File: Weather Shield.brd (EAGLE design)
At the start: 53.3 x 59.7 mm, 46 parts, among them J1 GP-635T, Q1 BSS138, Q2 BSS138, U1 ARDUINO_R3_SHIELD, U2 3.3V MIC5219, U3 ALS-PT19, U4 MPL3115A2LGA8, U5 HTU21D

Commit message: Initial commit
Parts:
- removed C1: 1uF, SparkFun:0603-CAP
- removed C13, C14: 10uF, SparkFun-Passives:EIA3216
- removed C2: 0.1uF, SparkFun:0603-CAP
- removed J1: GP-635T, SparkFun-Sensors:GP-635T
- removed JP2: External Batt Bckup, SparkFun-Connectors:1X02
- removed R10: 10K, SparkFun-Passives:0603-RES
- removed R7: 1K, SparkFun:0603-RES
- removed R8: 3.9K, SparkFun:0603-RES
- removed R9: 4.7K, SparkFun:0603-RES
- removed S2: Serial Select, SparkFun-Electromechanical:AYZ0202
- removed U1: ARDUINO_R3_SHIELD, SparkFun-Boards:UNO_R3_SHIELD
- removed U2: 3.3V MIC5219, SparkFun:SOT23-5
- removed U3: ALS-PT19, SparkFun-Sensors:ALS-PT19
- D1: value Blue -> Red
- moved JP10-DNP 50.6 mm to (52.1, 5.08), turned to 90 degrees
- moved LOGO1 46.6 mm to (3.81, 2.54)
- moved JP9-DNP 44.9 mm to (52.1, 21.6), turned to 90 degrees
- moved R16 37.6 mm to (36.8, 2.54), turned to 270 degrees
- moved R15 33.2 mm to (36.8, 6.35), turned to 270 degrees
- moved D9 32.7 mm to (39.4, 5.08), turned to 90 degrees
- moved R14 29.2 mm to (36.8, 10.2), turned to 90 degrees
- moved D10 28.2 mm to (39.4, 8.89), turned to 90 degrees
- moved R11 27.3 mm to (38.1, 26.7), turned to 270 degrees
- moved R12 25.9 mm to (35.6, 34.3), turned to 270 degrees
- moved R13 25.7 mm to (36.8, 14.0), turned to 270 degrees
- moved D7 24.1 mm to (39.4, 12.7), turned to 90 degrees
- moved R4 23.3 mm to (31.8, 12.7)
- moved Q1 23.3 mm to (31.8, 10.2)
- moved R17 22.9 mm to (36.8, 17.8), turned to 270 degrees
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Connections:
- removed net 3V_PWR_CTL: J1.6, R9.2
- removed net BATT_LVL: R7.1, R8.2, U1.A2
- removed net GPS-RX: J1.4, S2.2
- removed net GPS-TX: J1.3, S2.5
- removed net GRXI: S2.6, U1.D5
- removed net GTXO: S2.3, U1.D4
- removed net LIGHT: R10.2, U1.A1, U3.E
- removed net PWR_CTL: R9.1, U1.D6
- removed net RAW: C13.A, R8.1, U1.VIN, U2.1, U2.3
- removed net RXI: S2.4, U1.RX
- removed net TXO: S2.1, U1.TX
- removed net V_BATT: J1.5, JP2.2
- net 3.3V: no longer C1.1, C14.A, C2.1, J1.2, U1.A3, U2.5, U3.C
- net 5V: no longer U1.5V
- net GND: no longer C1.2, C13.C, C14.C, C2.2, J1.1, JP2.1, R10.1, R7.2, U1.GND@0, U1.GND@1, U1.GND@2, U2.2
- net HV_SCL: no longer U1.A5, U1.SCL
- net HV_SDA: no longer U1.A4, U1.SDA
- net RAIN: no longer U1.D2
- net STAT1: no longer U1.D7
- net STAT2: no longer U1.D8
- net WDIR: no longer U1.A0
- net WSPEED: no longer U1.D3
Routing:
- net 3.3V: track 131.2 -> 0.00 mm, vias 2 -> 0
- net HV_SCL: track 120.6 -> 0.00 mm, vias 3 -> 0
- net HV_SDA: track 113.8 -> 0.00 mm, vias 3 -> 0
- net PWR_CTL: track 63.3 -> 0.00 mm, vias 1 -> 0
- net RXI: track 61.7 -> 0.00 mm, vias 1 -> 0
- net BATT_LVL: track 55.7 -> 0.00 mm, vias 1 -> 0
- net TXO: track 54.6 -> 0.00 mm, vias 1 -> 0
- net RAW: track 52.5 -> 0.00 mm, vias 1 -> 0
- net 5V: track 49.1 -> 0.00 mm, vias 2 -> 0
- net GPS-RX: track 46.0 -> 0.00 mm
- net WSPEED: track 45.6 -> 0.00 mm
- net GND: track 44.7 -> 0.00 mm, vias 3 -> 0
- net GRXI: track 39.8 -> 0.00 mm, vias 1 -> 0
- net SDA: track 38.4 -> 0.00 mm, vias 2 -> 0
- net GTXO: track 37.8 -> 0.00 mm, vias 1 -> 0
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- removed copper zone on layer 1, net GND
- removed copper zone on layer 16, net GND
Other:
- board size 53.3 x 59.7 mm -> 57.1 x 38.1 mm
- board text added: "Weather Shield V1"
- board text removed: "+"
- board text removed: "-"
- board text removed: "Batt Bkup"
- board text removed: "GPS"
- board text removed: "Hard"
- board text removed: "Light"
- board text removed: "Serial"
- board text removed: "Soft"
- board text removed: "Weather Shield"
- board text removed: "v11"

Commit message: Initial commit
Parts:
- added PCB1: RASPBERRY_PI_B+_TPLACE, RASPBERRY_PI_Bplus:RASPBERRY_PI_BPLUS_TPLACE
- moved D3 65.4 mm to (62.2, 34.3), turned to 0 degrees
- moved R6 62.7 mm to (62.2, 30.5), turned to 90 degrees
- moved LOGO1 62.0 mm to (49.5, 44.5)
- moved D1 60.8 mm to (59.7, 34.3), turned to 0 degrees
- moved R1 57.8 mm to (59.7, 30.5), turned to 90 degrees
- moved JP10-DNP 54.7 mm to (5.08, 33.0), turned to 270 degrees
- moved JP9-DNP 47.3 mm to (5.08, 16.5), turned to 270 degrees
- moved C5 44.9 mm to (52.1, 31.8), turned to 0 degrees
- moved U5 41.8 mm to (52.1, 27.9), turned to 270 degrees
- moved C7 38.4 mm to (48.3, 31.8), turned to 0 degrees
- moved R16 36.9 mm to (20.3, 35.6), turned to 90 degrees
- moved D5 35.9 mm to (19.1, 3.81), turned to 90 degrees
- moved D9 35.3 mm to (17.8, 33.0), turned to 270 degrees
- moved R12 33.5 mm to (21.6, 3.81), turned to 90 degrees
- moved C6 32.4 mm to (44.5, 31.8), turned to 180 degrees
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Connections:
- new net 3V3: PCB1.1, PCB1.17
- new net 5V0: PCB1.2, PCB1.4
- net GND: now also PCB1.14, PCB1.20, PCB1.25, PCB1.30, PCB1.34, PCB1.39, PCB1.6, PCB1.9
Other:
- board size 57.1 x 38.1 mm -> 69.8 x 55.9 mm

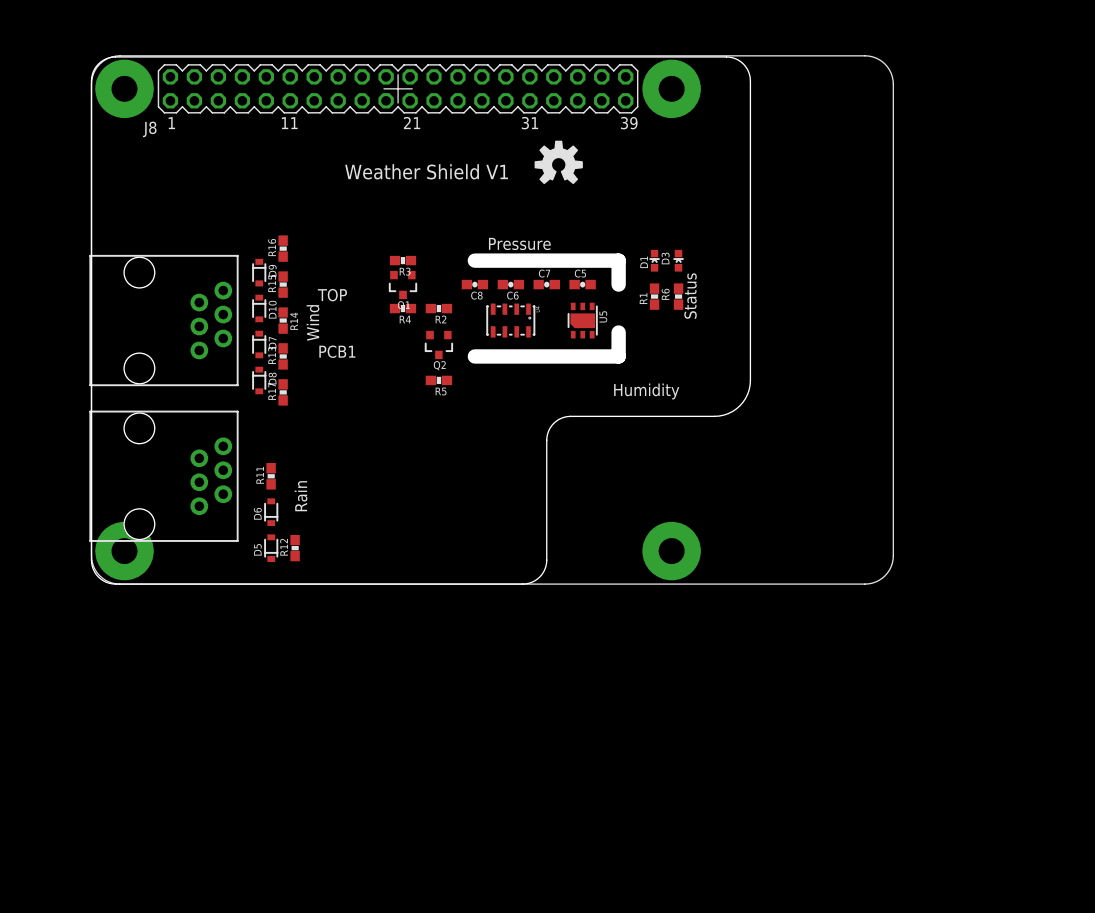
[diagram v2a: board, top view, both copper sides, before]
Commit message: FSE_Weather_Shield.lbr added
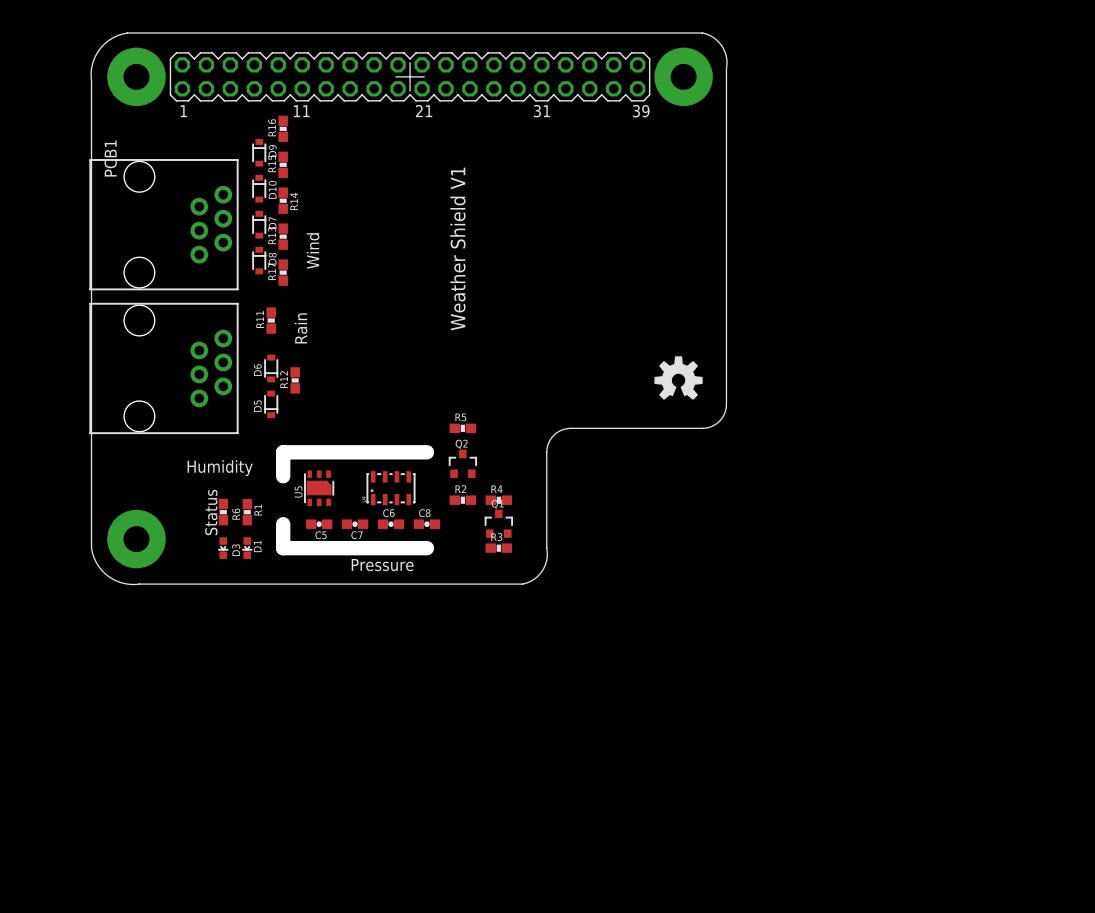
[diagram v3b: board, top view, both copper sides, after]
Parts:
- PCB1: value RASPBERRY_PI_B+_TPLACE -> RASPBERRY_PI_B+_DIM; device RASPBERRY_PI_Bplus:RASPBERRY_PI_BPLUS_TPLACE -> FSE_Weather_Shield:RASPBERRY_PI_BPLUS_DIM
- moved D3 57.1 mm to (14.0, 3.81), turned to 180 degrees
- moved R6 53.4 mm to (14.0, 7.62), turned to 270 degrees
- moved D1 52.9 mm to (16.5, 3.81), turned to 180 degrees
- moved R1 48.9 mm to (16.5, 7.62), turned to 270 degrees
- moved C5 37.8 mm to (24.1, 6.35), turned to 180 degrees
- moved U5 33.1 mm to (24.1, 10.2), turned to 90 degrees
- moved C7 32.5 mm to (27.9, 6.35), turned to 180 degrees
- moved R3 32.1 mm to (43.2, 3.81), turned to 0 degrees
- moved C6 28.4 mm to (31.8, 6.35), turned to 0 degrees
- moved Q1 27.4 mm to (43.2, 6.35), turned to 0 degrees
- moved LOGO1 26.2 mm to (62.2, 21.6)
- moved C8 25.9 mm to (35.6, 6.35), turned to 0 degrees
- moved R4 22.7 mm to (43.2, 8.89), turned to 0 degrees
- moved U4 21.8 mm to (31.8, 10.2), turned to 90 degrees
- moved R2 20.5 mm to (39.4, 8.89), turned to 0 degrees
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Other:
- board size 69.8 x 55.9 mm -> 15.2 x 10.2 mm

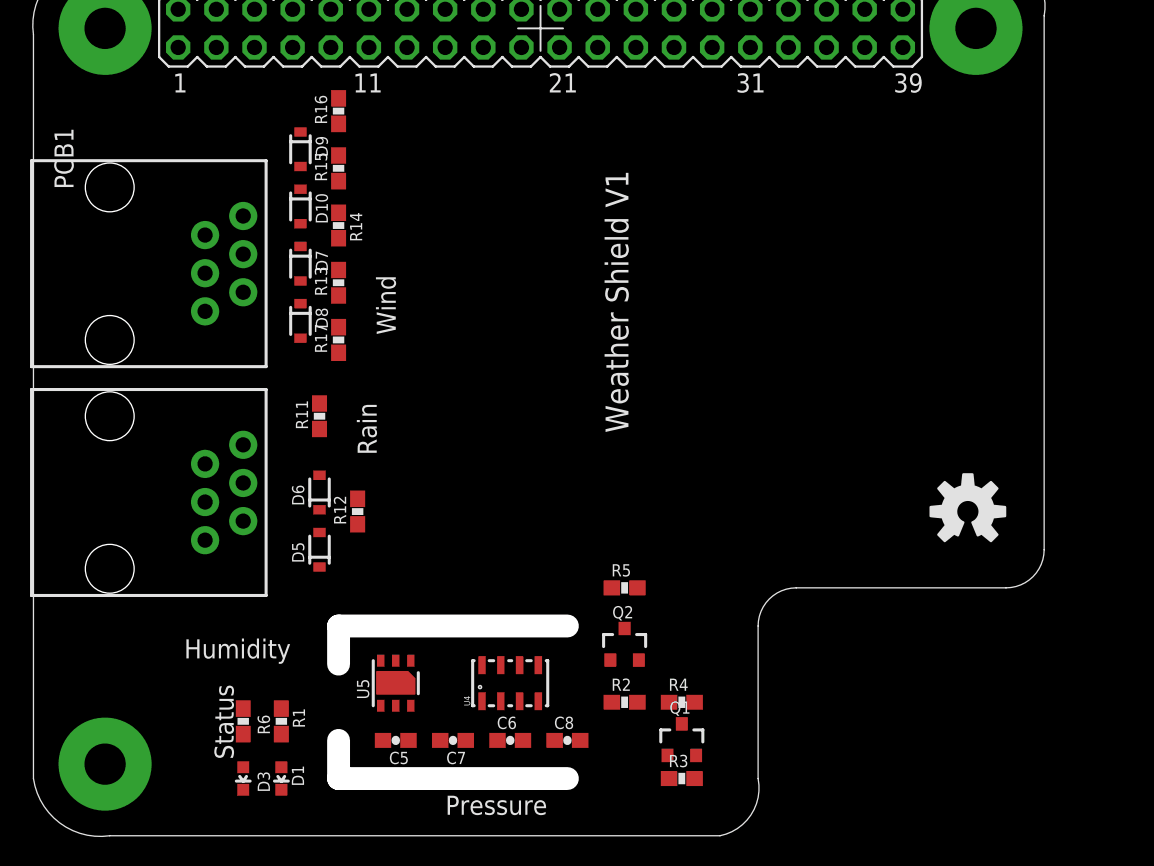
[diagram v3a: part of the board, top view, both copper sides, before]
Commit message: FSE_Weather_Shield.lbr added
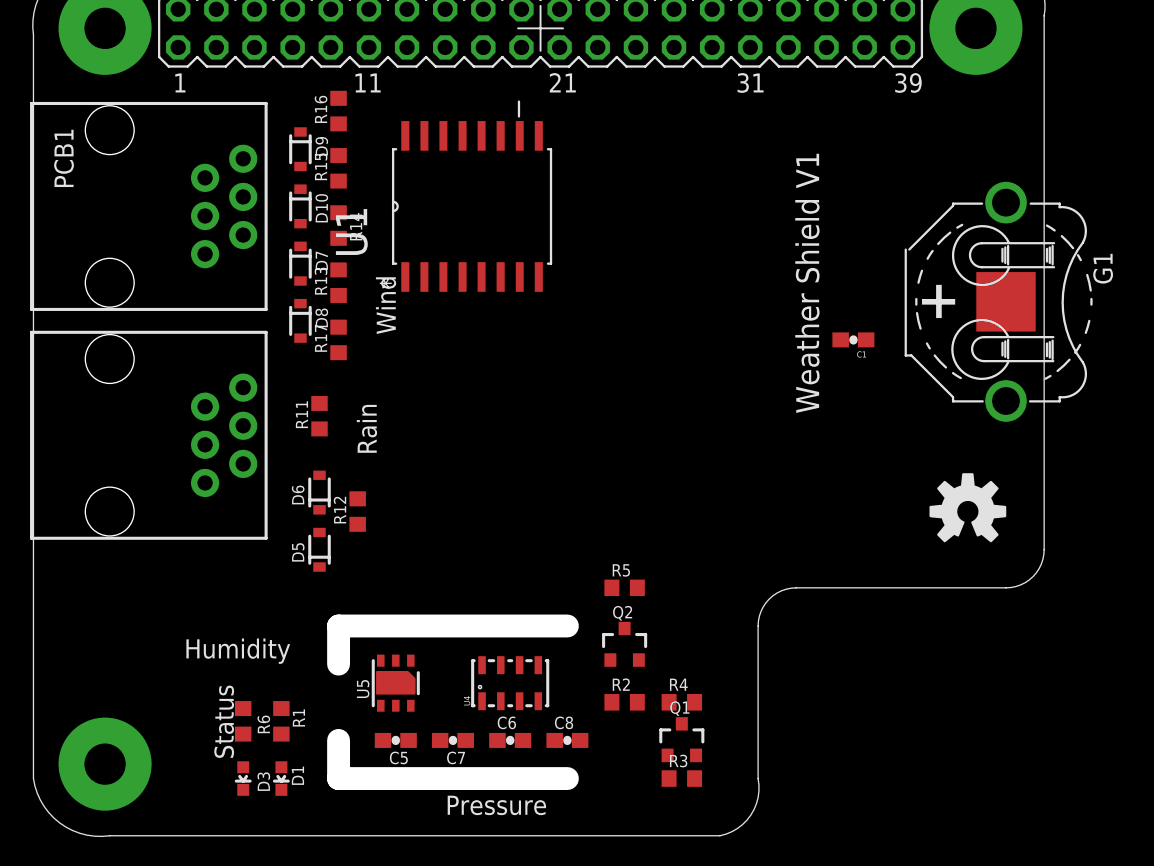
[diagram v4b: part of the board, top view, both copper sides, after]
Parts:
- added C1: 0.1uF, SparkFun:0603-CAP
- added G1: 3V, battery:CELL_RETAINER_11.6MM
- added U1: DS3231SN, FSE_Weather_Shield:SOIC127P1032X265-16N
- R1, R11, R12, R13, R14, R15, R16, R17, R2, R3, R4, R5, R6: device SparkFun:0603-RES -> rcl:R0603
- moved JP10-DNP 3.81 mm to (5.08, 47.0)
- moved JP9-DNP 3.81 mm to (5.08, 31.8)
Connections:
- new net N$6: G1.P+@1, G1.P+@2, U1.14
- new net VCC: C1.1, U1.2
- net GND: now also C1.2, G1.N-, U1.10, U1.11, U1.12, U1.13, U1.5, U1.6, U1.7, U1.8, U1.9

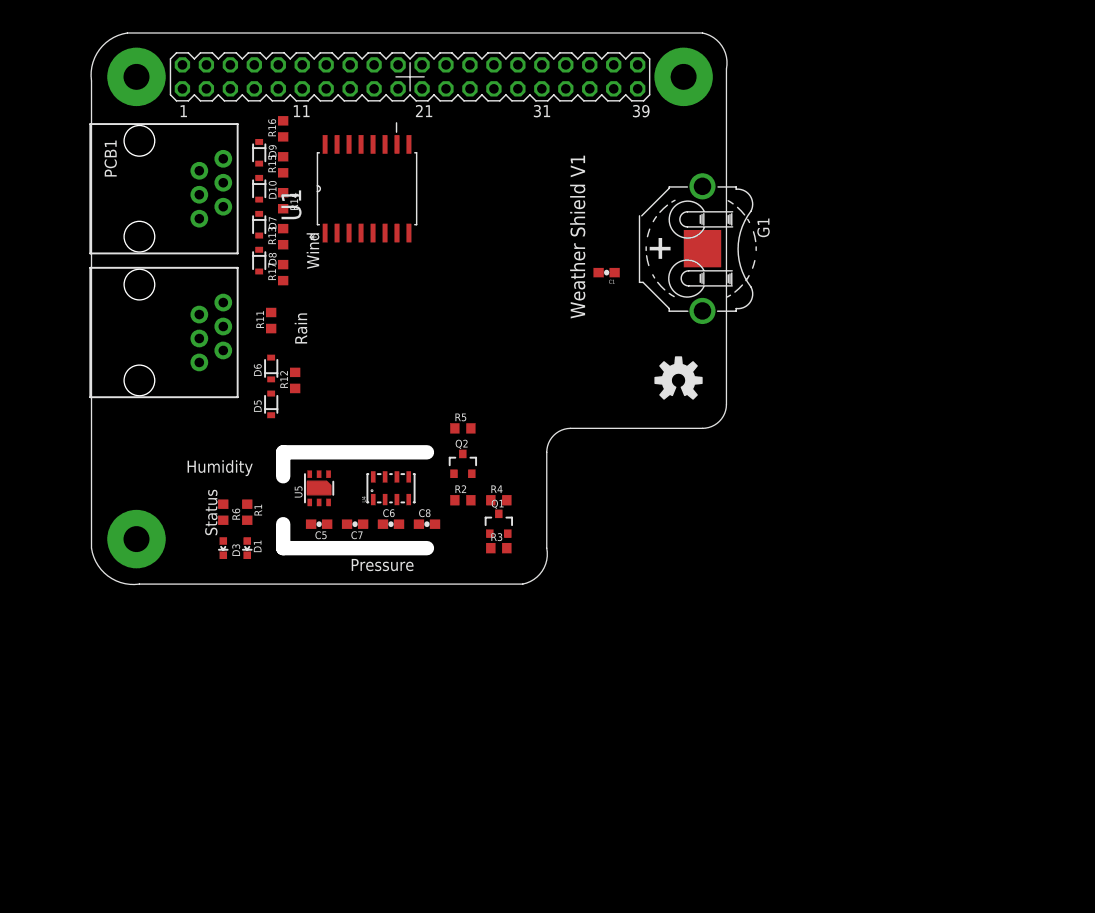
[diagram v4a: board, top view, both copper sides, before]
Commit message: FSE_Weather_Shield.lbr added
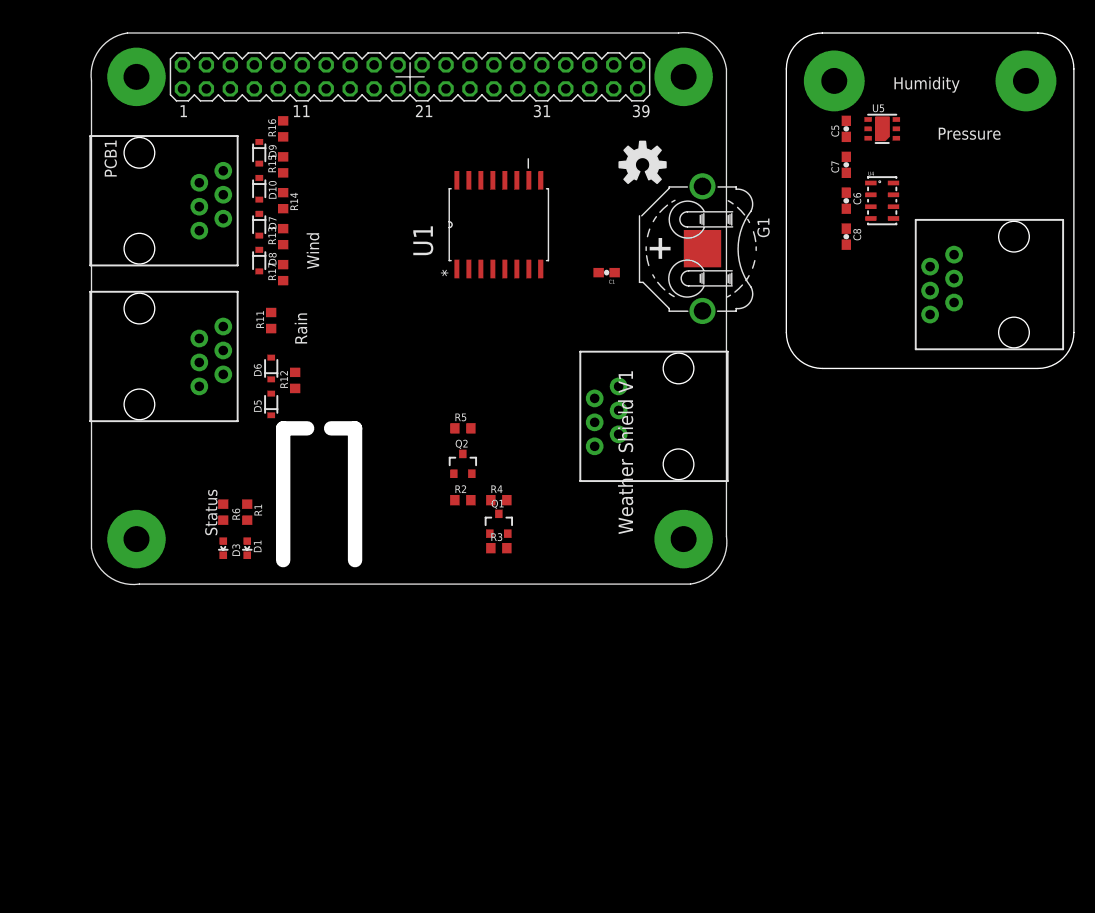
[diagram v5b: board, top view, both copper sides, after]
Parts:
- added JP9-DNP1, JP9-DNP2: RJ11-RAIN, SparkFun:RJ11-6
- PCB1: value RASPBERRY_PI_B+_DIM -> RASPBERRY_PI_B+/PI2_DIM
- moved U5 70.8 mm to (83.8, 48.3), turned to 0 degrees
- moved C5 69.8 mm to (80.0, 48.3), turned to 90 degrees
- moved C7 64.5 mm to (80.0, 44.5), turned to 90 degrees
- moved U4 60.3 mm to (83.8, 40.6), turned to 0 degrees
- moved C6 59.2 mm to (80.0, 40.6), turned to 270 degrees
- moved C8 53.9 mm to (80.0, 36.8), turned to 270 degrees
- moved LOGO1 23.2 mm to (58.4, 44.5)
- moved U1 14.5 mm to (43.2, 38.1)
- moved JP9-DNP 2.54 mm to (5.08, 29.2)
- moved JP10-DNP 1.27 mm to (5.08, 45.7)
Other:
- board size 15.2 x 10.2 mm -> 83.8 x 55.9 mm
